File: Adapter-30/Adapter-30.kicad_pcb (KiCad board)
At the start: 4 copper layers, 109.2 x 38.1 mm, 12 parts, among them J1 DRAM-SIMM-30, J2 IIfxRAM

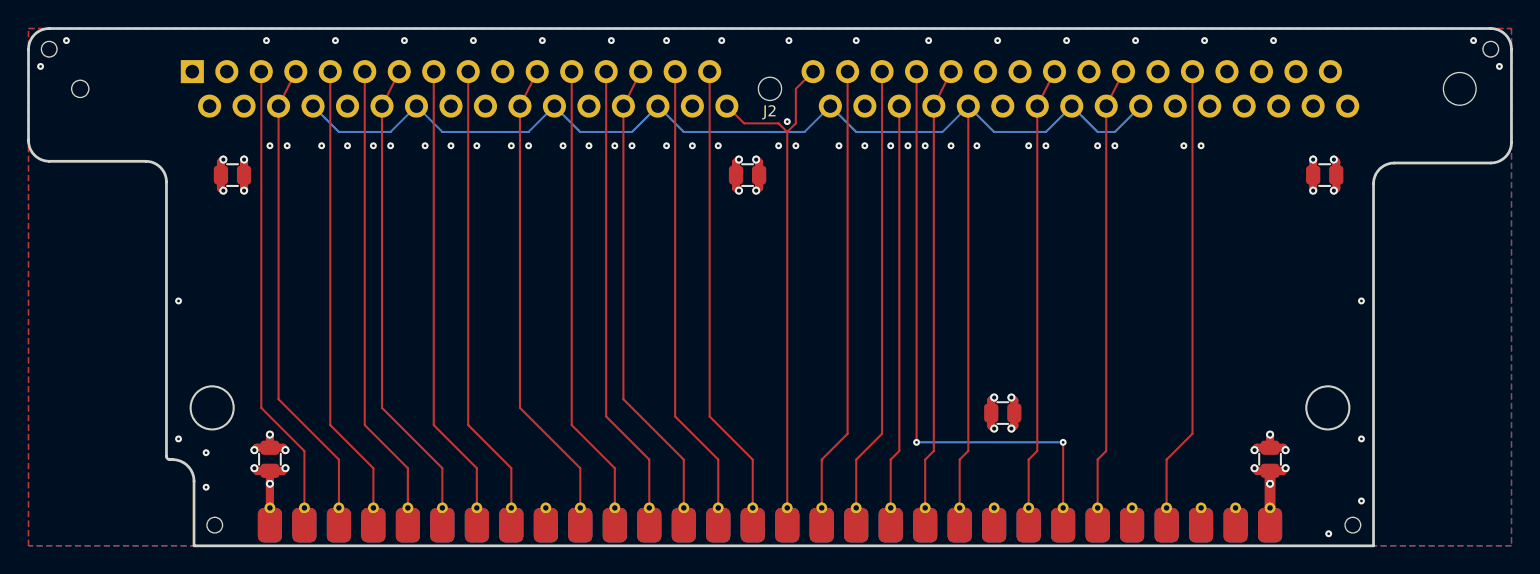
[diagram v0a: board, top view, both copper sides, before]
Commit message: Migrate to KiCAD 6
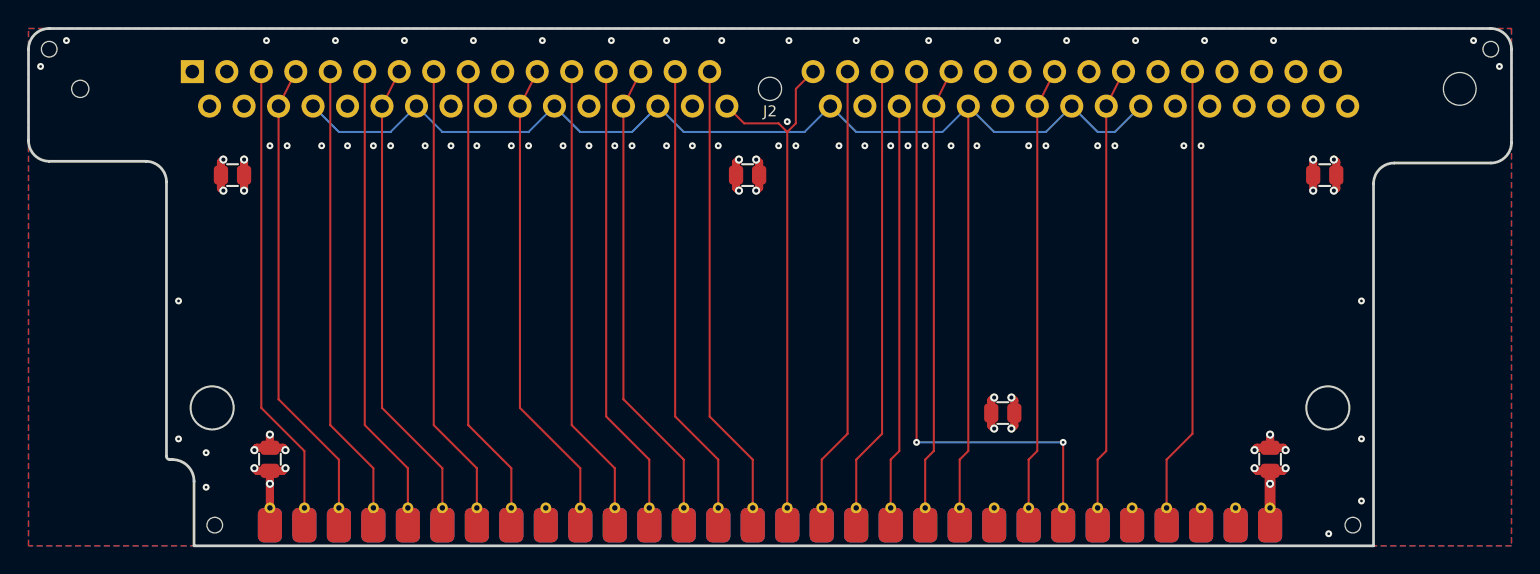
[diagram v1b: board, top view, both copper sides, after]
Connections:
- net /~CASP~ renamed /~{CASP}
- net /~CAS~ renamed /~{CAS}
- net /~Q~B renamed /~{Q}B
- net /~RAS~ renamed /~{RAS}
- net /~WE~ renamed /~{WE}
- net /~WWP~ renamed /~{WWP}
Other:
- outline, holes or cut-outs redrawn
- net class Default removed

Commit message: Prototype adapter-30
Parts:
- removed the C3 at (119.0, 74.3)
- removed C6: 2u2, stdpads:C_0805
- renumbered C5 to C2, C4 to C3, C2 to C4
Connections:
- J2 pad 10: Net-(J2-Pad10) -> unconnected-(J2-Pad10)
- J2 pad 16: Net-(J2-Pad16) -> unconnected-(J2-Pad16)
- J2 pad 2: Net-(J2-Pad2) -> unconnected-(J2-Pad2)
- J2 pad 24: Net-(J2-Pad24) -> unconnected-(J2-Pad24)
- J2 pad 30: Net-(J2-Pad30) -> unconnected-(J2-Pad30)
- J2 pad 36: Net-(J2-Pad36) -> unconnected-(J2-Pad36)
- J2 pad 43: Net-(J2-Pad43) -> unconnected-(J2-Pad43)
- J2 pad 44: Net-(J2-Pad44) -> unconnected-(J2-Pad44)
- J2 pad 49: Net-(J2-Pad49) -> unconnected-(J2-Pad49)
- J2 pad 54: Net-(J2-Pad54) -> unconnected-(J2-Pad54)
- J2 pad 56: Net-(J2-Pad56) -> unconnected-(J2-Pad56)
- J2 pad 57: Net-(J2-Pad57) -> unconnected-(J2-Pad57)
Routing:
- net +5V: track 20.8 -> 70.3 mm, vias 24 -> 0
- net GND: track 16.6 -> 11.7 mm, vias 66 -> 100
- net /A11: track 42.9 -> 43.2 mm, vias 2 -> 1
- added copper zone on B.Cu, net GND
- removed copper zone on B.Cu, net +5V
- removed copper zone on In1.Cu, net GND
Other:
- copper layers 4 -> 2
